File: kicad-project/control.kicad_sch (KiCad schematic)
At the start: 36 parts, among them SW1 RST_SW, U1 RP2040

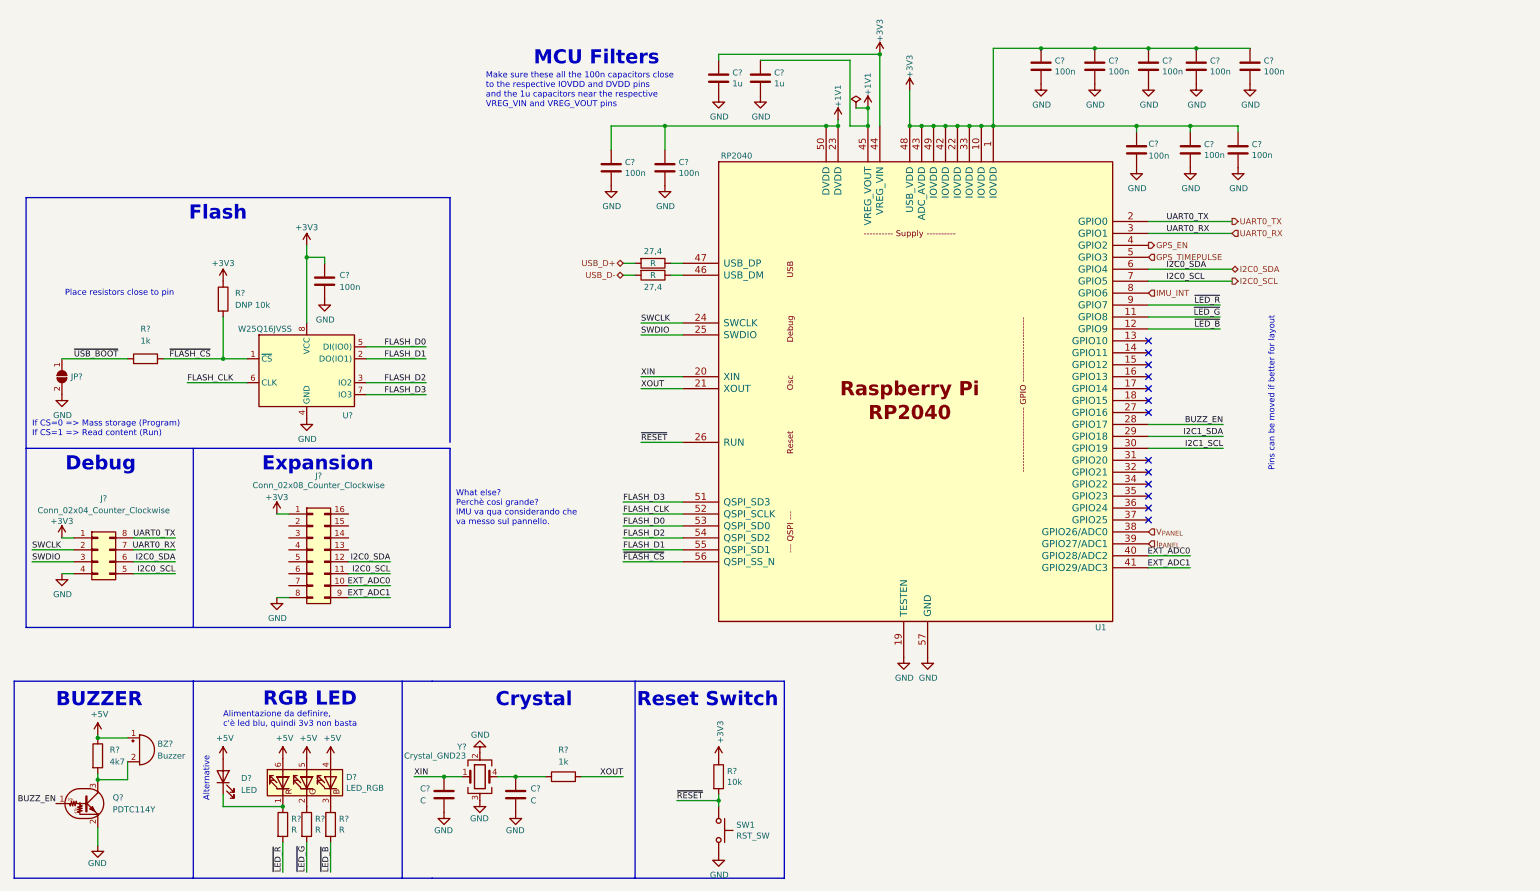
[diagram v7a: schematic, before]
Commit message: hw: added MAN_NORD and TRCK_ON_OFF buttons and OLED Display
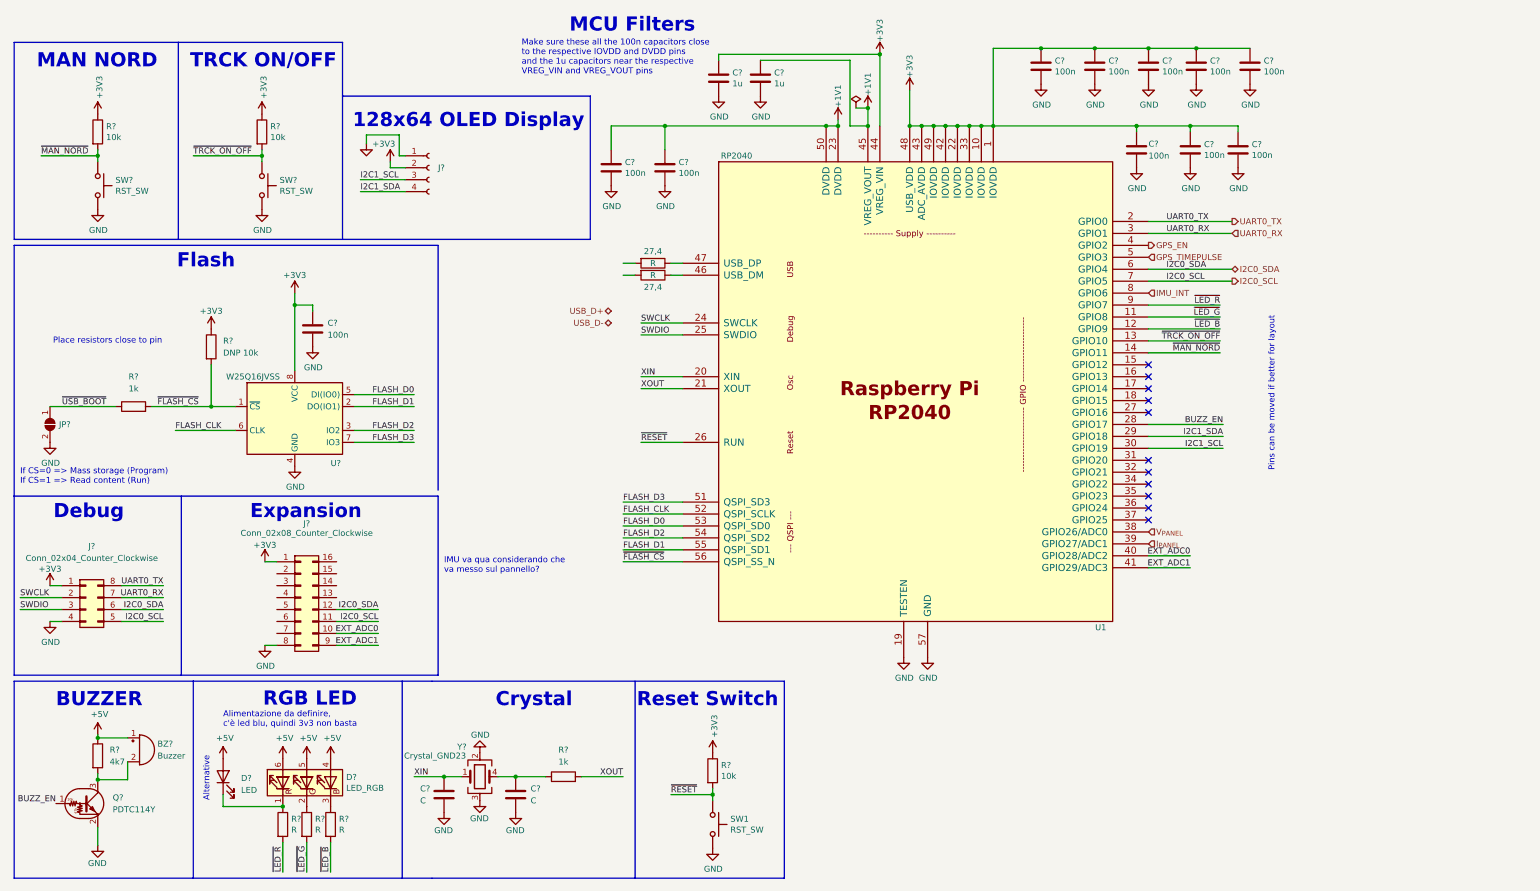
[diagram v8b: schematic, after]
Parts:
- added J?: (no value), symbol Connector:Conn_01x04_Female
- added R? (x2): 10k, symbol Device:R
- added SW? (x2): RST_SW, symbol Switch:SW_Push
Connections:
- net +3V3: now also J?.2 (Pin_2), R?.1, R?.1
- net GND: now also J?.1 (Pin_1), SW?.2, SW?.2
- net I2C1_SCL: now also J?.3 (Pin_3)
- net I2C1_SDA: now also J?.4 (Pin_4)
- net USB_D+: no longer 27,4.2
- net USB_D-: no longer 27,4.2
- net ~{TRCK_ON_OFF}: now reaches U1.13 (GPIO10)
- net ~{TRCK_ON_OFF}: now also R?.2, SW?.1
- net ~{MAN_NORD}: now reaches U1.14 (GPIO11)
- net ~{MAN_NORD}: now also R?.2, SW?.1
- no-connect marks 13 -> 11
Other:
- note added: "128x64 OLED Display"
- note added: "IMU va qua considerando che va messo sul pannello?"
- note added: "MAN NORD"
- note added: "TRCK ON/OFF"
- note removed: "What else? Perchè cosi grande? IMU va qua considerando che va messo sul pannello."
- moved on the sheet: C?, J?, JP?, R?, SW1, U?
